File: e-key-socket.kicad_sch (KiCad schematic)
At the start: 1 part, among them J2 MDT420E03002

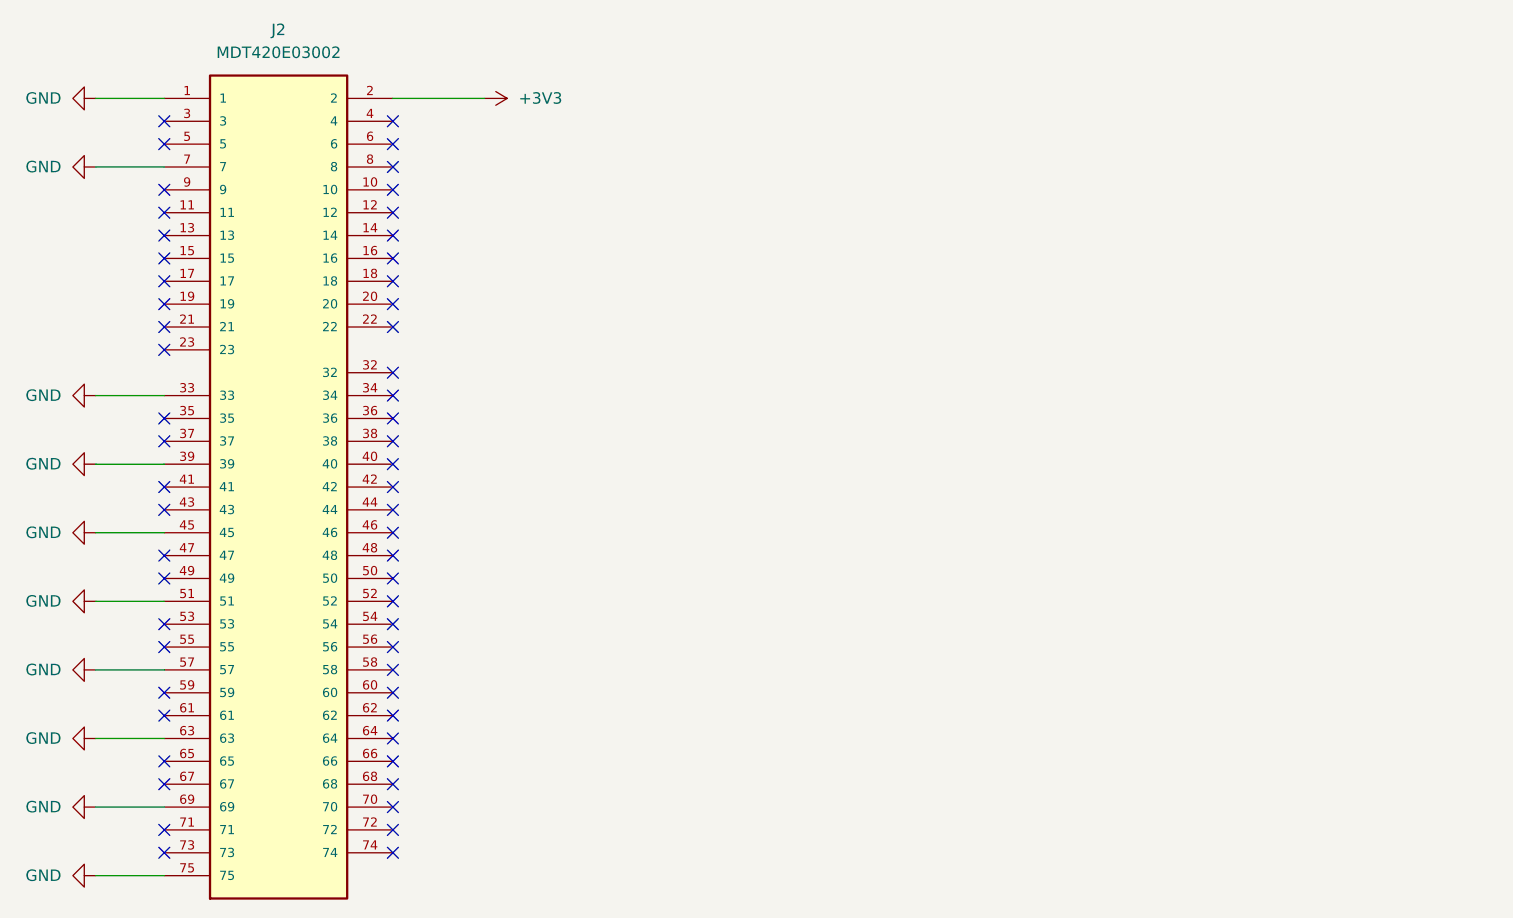
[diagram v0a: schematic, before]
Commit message: Replace dual holder with single holder
Signed-off-by: JeffMboya <jangina.mboya@gmail.com>
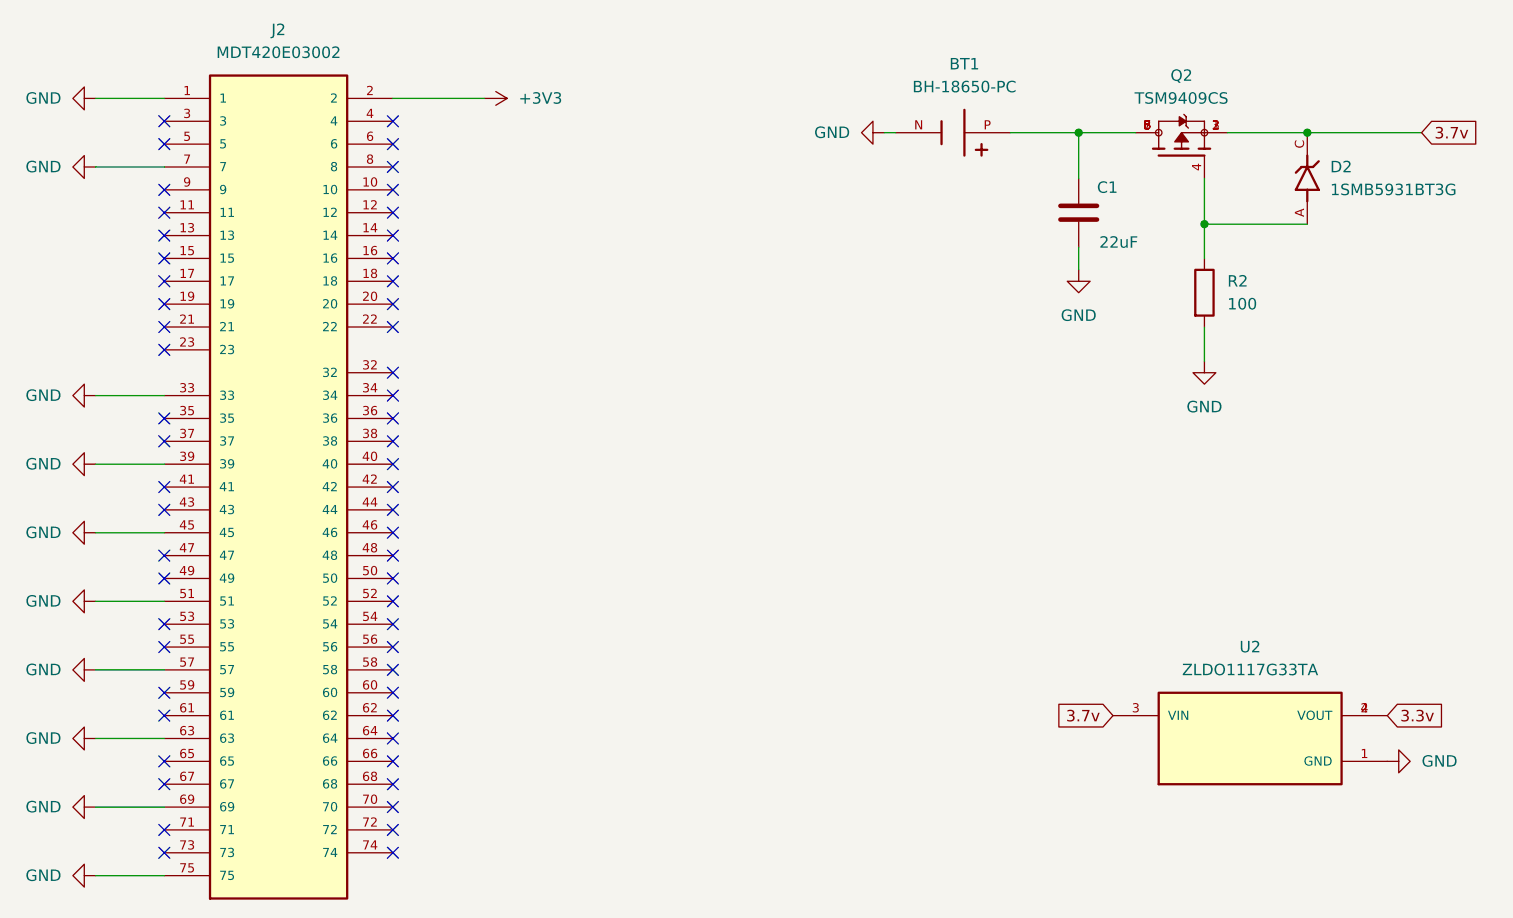
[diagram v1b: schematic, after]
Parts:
- added BT1: BH-18650-PC, BH-18650-PC:BAT_BH-18650-PC, symbol BH-18650-PC:BH-18650-PC
- added C1: 22uF, Capacitor_SMD:C_1206_3216Metric, symbol Device:C
- added D2: 1SMB5931BT3G, 1SMB5931BT3G:DIOM5436X247N, symbol 1SMB5931BT3G:1SMB5931BT3G
- added Q2: TSM9409CS, TSM9409CS:TRANS_TSM9409CS, symbol TSM9409CS:TSM9409CS
- added R2: 100, Resistor_SMD:R_0603_1608Metric, symbol Device:R
- added U2: ZLDO1117G33TA, ZLDO1117G33TA:SOT230P700X180-4N, symbol ZLDO1117G33TA:ZLDO1117G33TA
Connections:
- net GND: now also BT1.N, C1.2, R2.2, U2.1 (GND)
- new net: D2.A, Q2.4, R2.1
- new net: BT1.P, C1.1, Q2.5, Q2.6, Q2.7, Q2.8
- new net 3.3v: U2.2 (VOUT), U2.4 (VOUT)
- new net 3.7v: D2.C, Q2.1, Q2.2, Q2.3, U2.3 (VIN)
